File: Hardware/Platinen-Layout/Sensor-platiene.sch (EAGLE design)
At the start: 38 parts, among them J10 Flash Programming, J5 Flash Programming, U1 AS72651, U10 4MB Flash, U2 4MB Flash, U5 AS72653, U6 AS72652

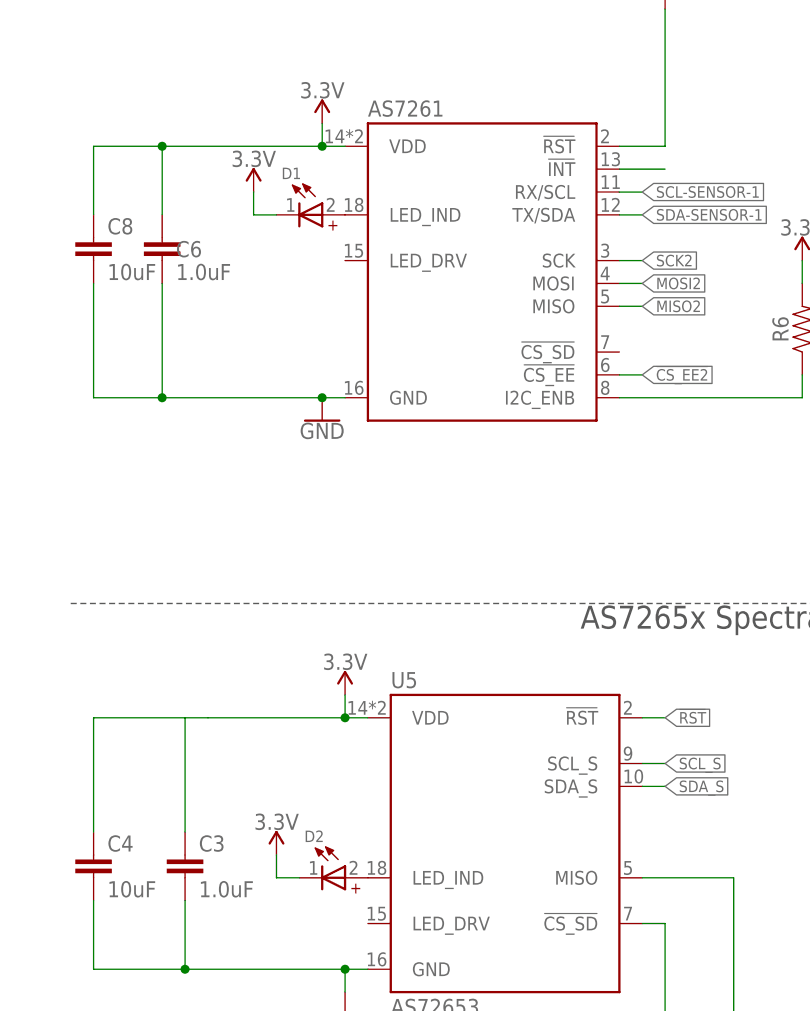
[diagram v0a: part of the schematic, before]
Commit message: add write to db
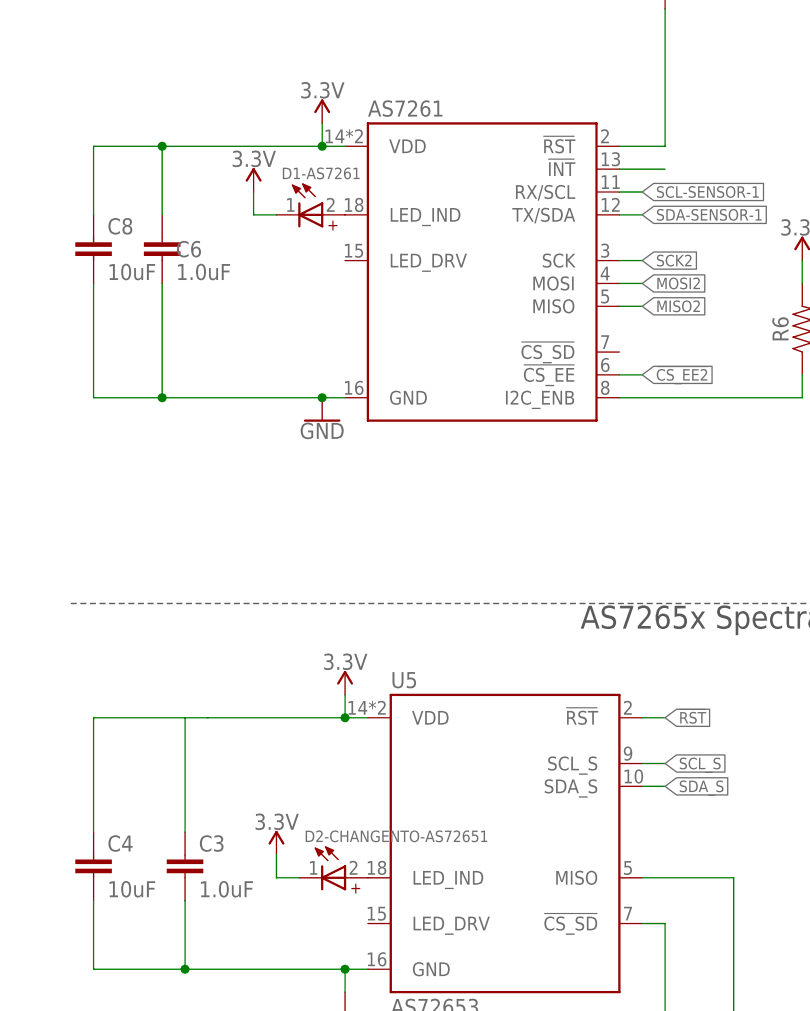
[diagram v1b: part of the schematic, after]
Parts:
- renumbered D1 to D1-AS7261, D2 to D2-CHANGENTO-AS72651
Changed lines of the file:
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@@
 <?xml version="1.0" encoding="utf-8"?>
 <!DOCTYPE eagle SYSTEM "eagle.dtd">
-<eagle version="9.6.1">
+<eagle version="9.6.2">
 <drawing>
 <settings>
@@
 <part name="SUPPLY2" library="SparkFun-PowerSymbols" deviceset="3.3V" device=""/>
 <part name="SUPPLY5" library="SparkFun-PowerSymbols" deviceset="3.3V" device=""/>
-<part name="D1" library="150120RS75000_Eagle_WL-SMCW_rev20b" deviceset="WL-SMCW_1206" device="" package3d_urn="urn:adsk.eagle:package:19028166/2" technology="_150120RS75000"/>
-<part name="D2" library="150120RS75000_Eagle_WL-SMCW_rev20b" deviceset="WL-SMCW_1206" device="" package3d_urn="urn:adsk.eagle:package:19028166/2" technology="_150120RS75000"/>
+<part name="D1-AS7261" library="150120RS75000_Eagle_WL-SMCW_rev20b" deviceset="WL-SMCW_1206" device="" package3d_urn="urn:adsk.eagle:package:19028166/2" technology="_150120RS75000"/>
+<part name="D2-CHANGENTO-AS72651" library="150120RS75000_Eagle_WL-SMCW_rev20b" deviceset="WL-SMCW_1206" device="" package3d_urn="urn:adsk.eagle:package:19028166/2" technology="_150120RS75000"/>
 <part name="SUPPLY10" library="SparkFun-PowerSymbols" deviceset="3.3V" device=""/>
 <part name="SUPPLY15" library="SparkFun-PowerSymbols" deviceset="3.3V" device=""/>
@@
 <attribute name="VALUE" x="30.48" y="221.234" size="1.778" layer="96" align="bottom-center"/>
 </instance>
-<instance part="D1" gate="G$1" x="35.56" y="215.9" smashed="yes">
+<instance part="D1-AS7261" gate="G$1" x="35.56" y="215.9" smashed="yes">
 <attribute name="NAME" x="33.572" y="219.872" size="1.27" layer="95"/>
 <attribute name="VALUE" x="32.932" y="211.972" size="1.27" layer="96"/>
 </instance>
-<instance part="D2" gate="G$1" x="38.1" y="142.24" smashed="yes">
+<instance part="D2-CHANGENTO-AS72651" gate="G$1" x="38.1" y="142.24" smashed="yes">
 <attribute name="NAME" x="36.112" y="146.212" size="1.27" layer="95"/>
 <attribute name="VALUE" x="35.472" y="138.312" size="1.27" layer="96"/>
@@
 <wire x1="33.02" y1="142.24" x2="33.02" y2="144.78" width="0.1524" layer="91"/>
 <pinref part="SUPPLY2" gate="G$1" pin="3.3V"/>
-<pinref part="D2" gate="G$1" pin="-"/>
+<pinref part="D2-CHANGENTO-AS72651" gate="G$1" pin="-"/>
 </segment>
 <segment>
@@
 <wire x1="30.48" y1="215.9" x2="30.48" y2="218.44" width="0.1524" layer="91"/>
 <pinref part="SUPPLY5" gate="G$1" pin="3.3V"/>
-<pinref part="D1" gate="G$1" pin="-"/>
+<pinref part="D1-AS7261" gate="G$1" pin="-"/>
 </segment>
 <segment>
@@
 <segment>
 <pinref part="AS7261" gate="U1" pin="LED_IND"/>
-<pinref part="D1" gate="G$1" pin="+"/>
+<pinref part="D1-AS7261" gate="G$1" pin="+"/>
 </segment>
 </net>
@@
 <segment>
 <pinref part="U5" gate="U1" pin="LED_IND"/>
-<pinref part="D2" gate="G$1" pin="+"/>
-</segment>
-</net>
+<pinref part="D2-CHANGENTO-AS72651" gate="G$1" pin="+"/>
+</segment>
+</net>
